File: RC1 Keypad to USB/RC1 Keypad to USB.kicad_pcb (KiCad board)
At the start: 2 copper layers, 72.4 x 45.1 mm, 8 parts, among them J1 RC1 Keypad Port, J2 Anchor, SW1 RESET

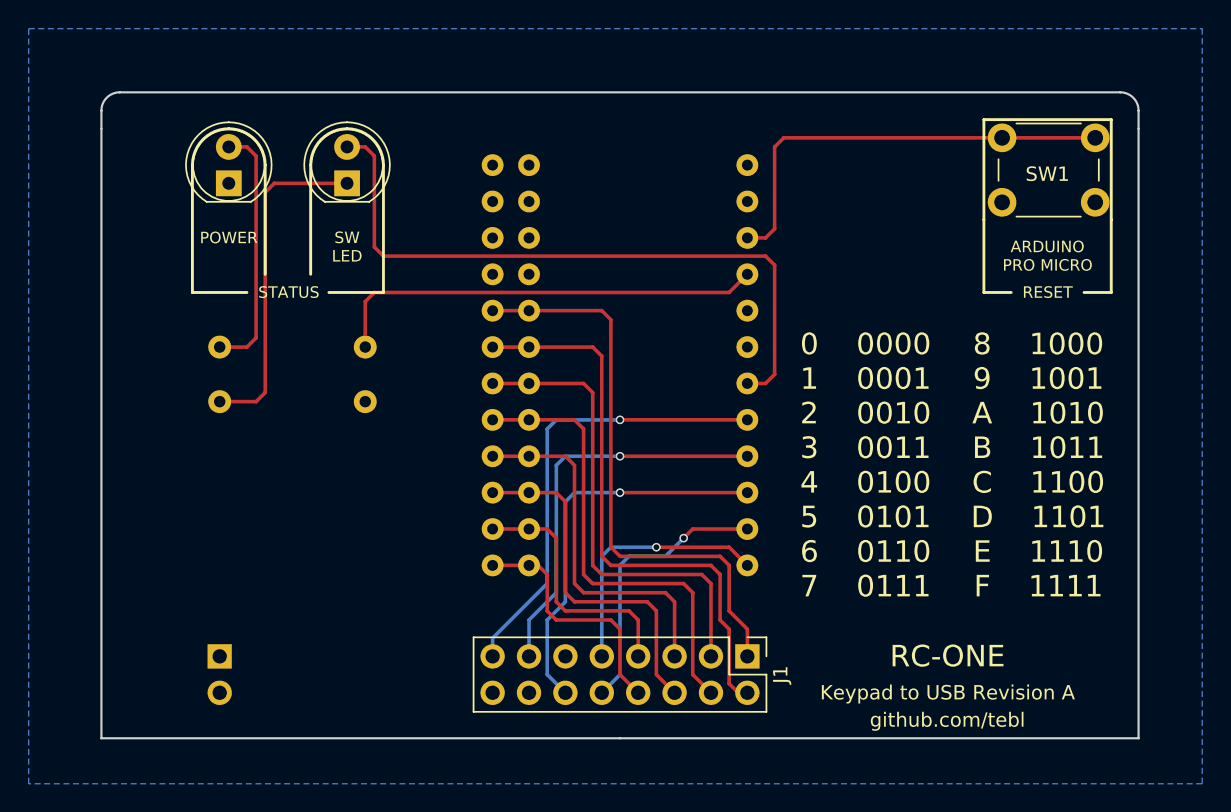
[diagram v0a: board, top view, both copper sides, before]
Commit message: Gerber export keypad to USB module
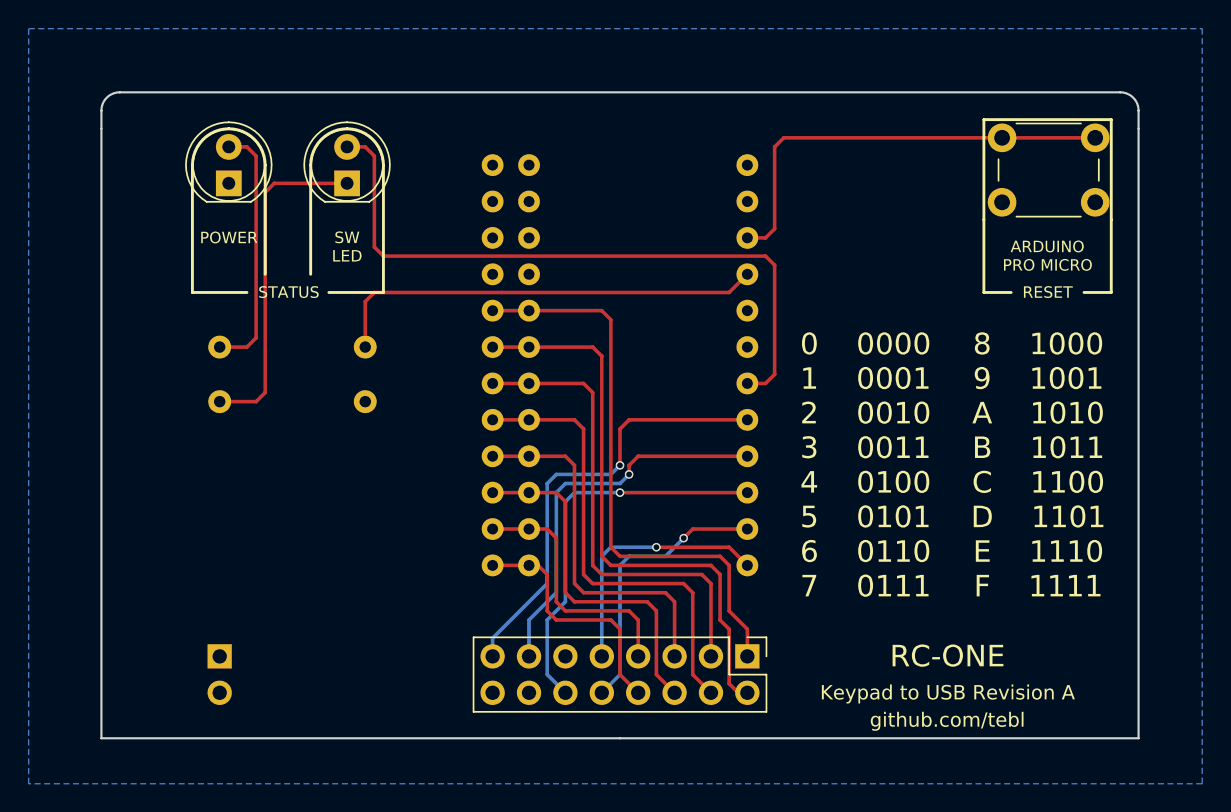
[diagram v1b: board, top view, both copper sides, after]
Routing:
- net /D18: track 31.7 -> 30.9 mm
- net /D15: track 27.7 -> 27.0 mm
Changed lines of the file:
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@@
     (links 37)
     (no_connects 0)
-    (area 112.395 94.615 194.310001 147.320001)
+    (area 117.399999 98.984999 189.940001 144.220001)
     (thickness 1.6)
     (drawings 38)
-    (tracks 145)
+    (tracks 150)
     (zones 0)
     (modules 8)
@@
     (descr "Through hole straight pin header, 2x08, 2.54mm pitch, double rows")
     (tags "Through hole pin header THT 2x08 2.54mm double row")
-    (fp_text reference J1 (at 1.27 -2.33 270) (layer F.SilkS)
+    (fp_text reference J1 (at 1.27 -2.54 270) (layer F.Fab)
       (effects (font (size 1 1) (thickness 0.15)))
     )
@@
     (descr https://www.omron.com/ecb/products/pdf/en-b3f.pdf)
     (tags "tact sw push 6mm")
-    (fp_text reference SW1 (at 3.175 2.54) (layer F.SilkS)
-      (effects (font (size 1 1) (thickness 0.15)))
-    )
-    (fp_text value RESET (at 3.75 6.7) (layer F.Fab)
+    (fp_text reference SW1 (at 3.175 2.54) (layer F.Fab)
+      (effects (font (size 1 1) (thickness 0.15)))
+    )
+    (fp_text value RESET (at 3.175 6.985) (layer F.Fab)
       (effects (font (size 1 1) (thickness 0.15)))
     )
@@
   (segment (start 153.67 139.7) (end 153.67 132.08) (width 0.25) (layer B.Cu) (net 11))
   (via (at 153.67 127) (size 0.6) (drill 0.4) (layers F.Cu B.Cu) (net 12))
-  (segment (start 153.67 127) (end 162.56 127) (width 0.25) (layer F.Cu) (net 12) (status 800000))
+  (segment (start 153.67 127) (end 162.56 127) (width 0.25) (layer F.Cu) (net 12))
   (segment (start 153.67 127) (end 150.495 127) (width 0.25) (layer B.Cu) (net 12))
   (segment (start 148.59 139.7) (end 149.86 140.97) (width 0.25) (layer B.Cu) (net 12))
@@
   (segment (start 149.86 127.635) (end 149.86 134.62) (width 0.25) (layer B.Cu) (net 12))
   (segment (start 150.495 127) (end 149.86 127.635) (width 0.25) (layer B.Cu) (net 12))
-  (via (at 153.67 124.46) (size 0.6) (drill 0.4) (layers F.Cu B.Cu) (net 13))
-  (segment (start 153.67 124.46) (end 162.56 124.46) (width 0.25) (layer F.Cu) (net 13) (status 800000))
+  (segment (start 149.225 127) (end 149.86 126.365) (width 0.25) (layer B.Cu) (net 13))
+  (segment (start 154.305 125.095) (end 154.94 124.46) (width 0.25) (layer F.Cu) (net 13))
+  (segment (start 154.305 125.73) (end 154.305 125.095) (width 0.25) (layer F.Cu) (net 13))
+  (via (at 154.305 125.73) (size 0.6) (drill 0.4) (layers F.Cu B.Cu) (net 13))
+  (segment (start 153.67 126.365) (end 154.305 125.73) (width 0.25) (layer B.Cu) (net 13))
+  (segment (start 149.86 126.365) (end 153.67 126.365) (width 0.25) (layer B.Cu) (net 13))
+  (segment (start 154.94 124.46) (end 162.56 124.46) (width 0.25) (layer F.Cu) (net 13))
   (segment (start 148.59 134.62) (end 147.32 135.89) (width 0.25) (layer B.Cu) (net 13))
   (segment (start 147.32 138.43) (end 147.32 135.89) (width 0.25) (layer B.Cu) (net 13))
-  (segment (start 149.86 124.46) (end 153.67 124.46) (width 0.25) (layer B.Cu) (net 13))
-  (segment (start 149.225 125.095) (end 149.86 124.46) (width 0.25) (layer B.Cu) (net 13))
-  (segment (start 149.225 133.985) (end 149.225 125.095) (width 0.25) (layer B.Cu) (net 13))
+  (segment (start 149.225 133.985) (end 149.225 127) (width 0.25) (layer B.Cu) (net 13))
   (segment (start 148.59 134.62) (end 149.225 133.985) (width 0.25) (layer B.Cu) (net 13))
+  (segment (start 148.59 126.365) (end 149.225 125.73) (width 0.25) (layer B.Cu) (net 14))
+  (segment (start 153.67 122.555) (end 154.305 121.92) (width 0.25) (layer F.Cu) (net 14))
+  (segment (start 153.67 125.095) (end 153.67 122.555) (width 0.25) (layer F.Cu) (net 14))
+  (via (at 153.67 125.095) (size 0.6) (drill 0.4) (layers F.Cu B.Cu) (net 14))
+  (segment (start 153.035 125.73) (end 153.67 125.095) (width 0.25) (layer B.Cu) (net 14))
+  (segment (start 149.225 125.73) (end 153.035 125.73) (width 0.25) (layer B.Cu) (net 14))
   (segment (start 147.955 133.985) (end 144.78 137.16) (width 0.25) (layer B.Cu) (net 14))
-  (segment (start 162.56 121.92) (end 153.67 121.92) (width 0.25) (layer F.Cu) (net 14))
+  (segment (start 162.56 121.92) (end 154.305 121.92) (width 0.25) (layer F.Cu) (net 14))
   (segment (start 144.78 137.16) (end 144.78 138.43) (width 0.25) (layer B.Cu) (net 14))
   (segment (start 148.59 133.35) (end 147.955 133.985) (width 0.25) (layer B.Cu) (net 14))
-  (segment (start 148.59 122.555) (end 148.59 133.35) (width 0.25) (layer B.Cu) (net 14))
-  (segment (start 149.225 121.92) (end 148.59 122.555) (width 0.25) (layer B.Cu) (net 14))
-  (segment (start 149.86 121.92) (end 149.225 121.92) (width 0.25) (layer B.Cu) (net 14))
-  (segment (start 153.67 121.92) (end 149.86 121.92) (width 0.25) (layer B.Cu) (net 14))
-  (via (at 153.67 121.92) (size 0.6) (drill 0.4) (layers F.Cu B.Cu) (net 14))
+  (segment (start 148.59 126.365) (end 148.59 133.35) (width 0.25) (layer B.Cu) (net 14))
   (segment (start 162.56 119.38) (end 163.83 119.38) (width 0.25) (layer F.Cu) (net 15))
   (segment (start 135.89 102.87) (end 134.62 102.87) (width 0.25) (layer F.Cu) (net 15))

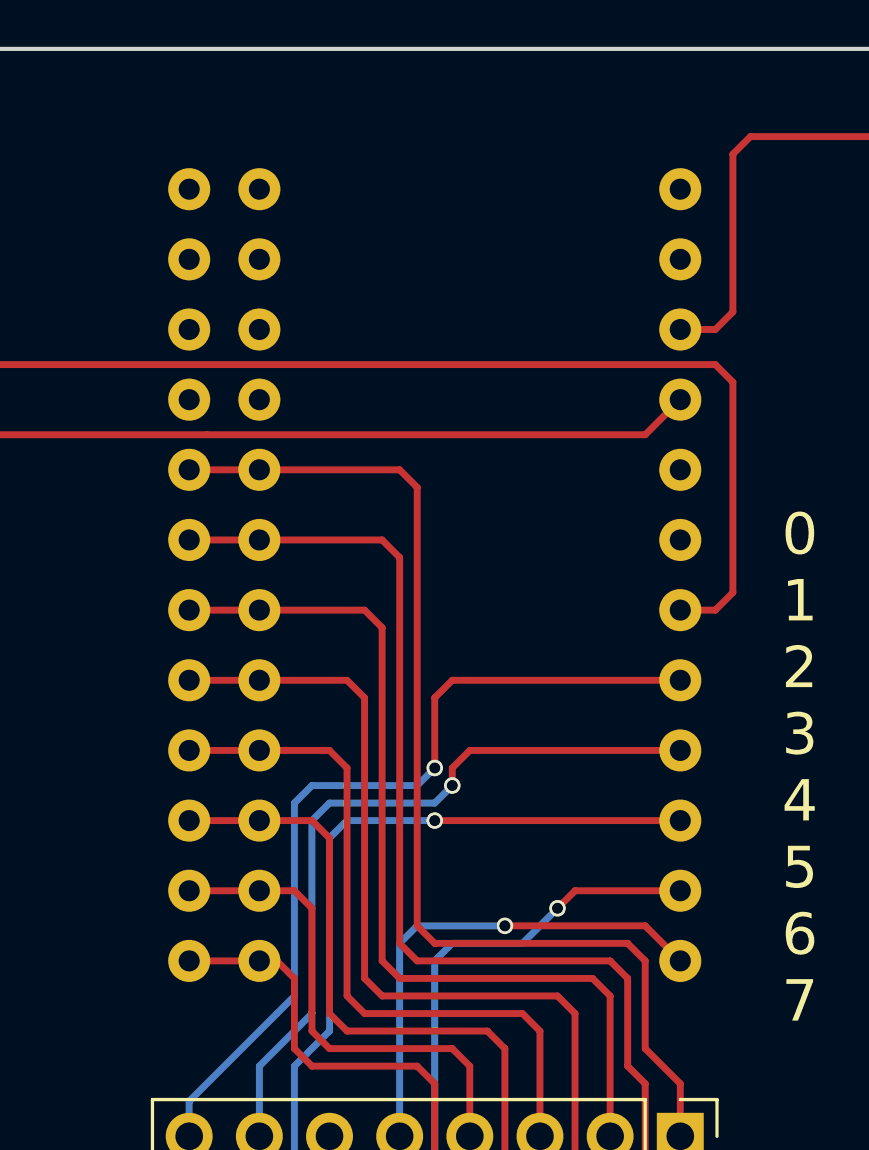
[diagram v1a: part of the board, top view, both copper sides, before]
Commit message: Updated pad dimensions for Arduino Pro Micro
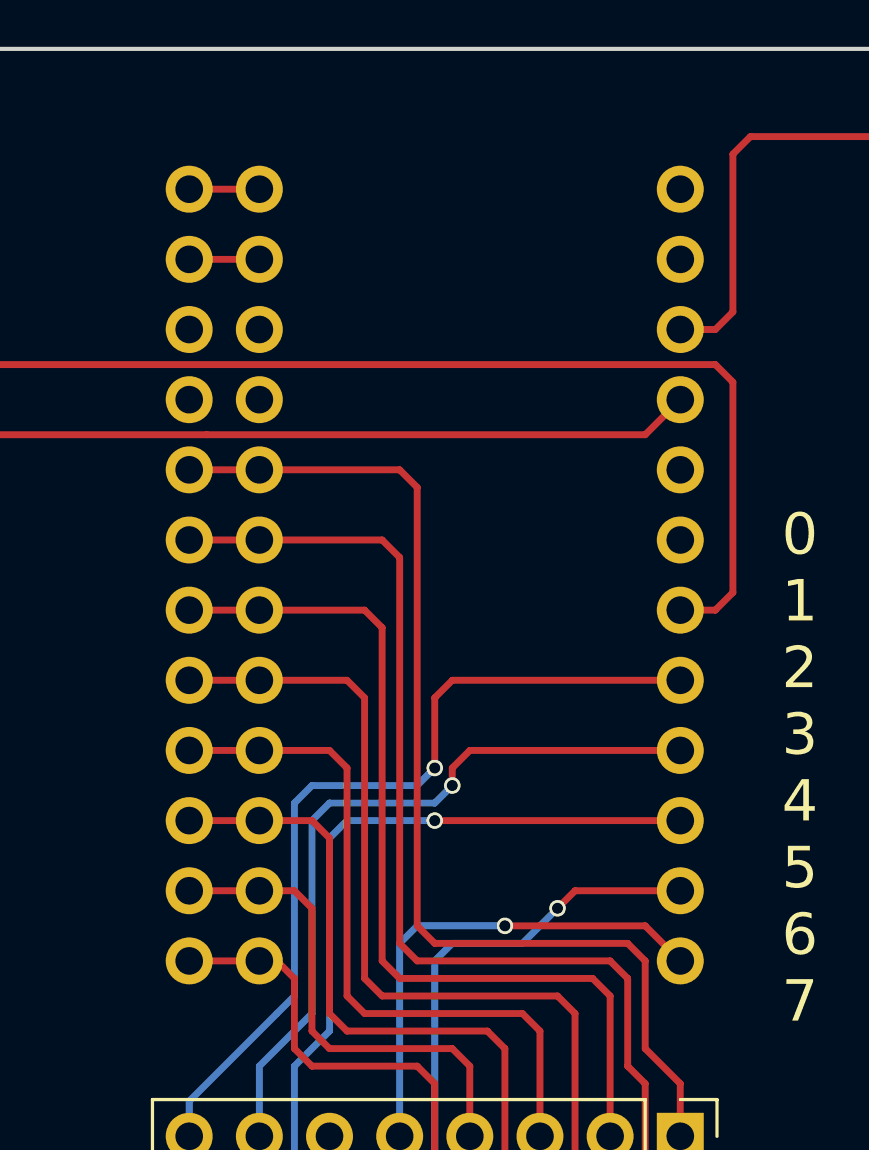
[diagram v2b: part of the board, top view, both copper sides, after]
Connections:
- A1 pad 1: (no net) -> Net-(A1-Pad1)
- A1 pad 2: (no net) -> Net-(A1-Pad2)
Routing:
- net Net-(A1-Pad2): track 0.00 -> 2.54 mm
- net Net-(A1-Pad1): track 0.00 -> 2.54 mm
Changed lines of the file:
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@@
 (kicad_pcb (version 4) (host pcbnew 4.0.7)
   (general
-    (links 37)
+    (links 39)
     (no_connects 0)
     (area 117.399999 98.984999 189.940001 144.220001)
     (thickness 1.6)
     (drawings 38)
-    (tracks 150)
+    (tracks 152)
     (zones 0)
     (modules 8)
-    (nets 20)
+    (nets 22)
   )
   (page A4)
@@
   (net 18 "Net-(D1-Pad2)")
   (net 19 "Net-(D2-Pad1)")
+  (net 20 "Net-(A1-Pad2)")
+  (net 21 "Net-(A1-Pad1)")
   (net_class Default "This is the default net class."
     (clearance 0.2)
@@
     (add_net /D9)
     (add_net GND)
+    (add_net "Net-(A1-Pad1)")
     (add_net "Net-(A1-Pad18)")
+    (add_net "Net-(A1-Pad2)")
     (add_net "Net-(A1-Pad21)")
     (add_net "Net-(A1-Pad22)")
@@
     (fp_line (start -10.16 -17.78) (end -10.16 16.51) (layer B.SilkS) (width 0.15))
     (fp_line (start -10.16 16.51) (end 10.16 16.51) (layer B.SilkS) (width 0.15))
-    (pad 12 thru_hole circle (at -6.35 13.97) (size 1.524 1.524) (drill 0.762) (layers *.Cu *.Mask)
+    (pad 12 thru_hole circle (at -6.35 13.97) (size 1.7 1.7) (drill 1) (layers *.Cu *.Mask)
       (net 9 /D9))
-    (pad 11 thru_hole circle (at -6.35 11.43) (size 1.524 1.524) (drill 0.762) (layers *.Cu *.Mask)
+    (pad 11 thru_hole circle (at -6.35 11.43) (size 1.7 1.7) (drill 1) (layers *.Cu *.Mask)
       (net 8 /D8))
-    (pad 10 thru_hole circle (at -6.35 8.89) (size 1.524 1.524) (drill 0.762) (layers *.Cu *.Mask)
+    (pad 10 thru_hole circle (at -6.35 8.89) (size 1.7 1.7) (drill 1) (layers *.Cu *.Mask)
       (net 7 /D7))
-    (pad 9 thru_hole circle (at -6.35 6.35) (size 1.524 1.524) (drill 0.762) (layers *.Cu *.Mask)
+    (pad 9 thru_hole circle (at -6.35 6.35) (size 1.7 1.7) (drill 1) (layers *.Cu *.Mask)
       (net 6 /D6))
-    (pad 8 thru_hole circle (at -6.35 3.81) (size 1.524 1.524) (drill 0.762) (layers *.Cu *.Mask)
+    (pad 8 thru_hole circle (at -6.35 3.81) (size 1.7 1.7) (drill 1) (layers *.Cu *.Mask)
       (net 5 /D5))
-    (pad 7 thru_hole circle (at -6.35 1.27) (size 1.524 1.524) (drill 0.762) (layers *.Cu *.Mask)
+    (pad 7 thru_hole circle (at -6.35 1.27) (size 1.7 1.7) (drill 1) (layers *.Cu *.Mask)
       (net 4 /D4))
-    (pad 6 thru_hole circle (at -6.35 -1.27) (size 1.524 1.524) (drill 0.762) (layers *.Cu *.Mask)
+    (pad 6 thru_hole circle (at -6.35 -1.27) (size 1.7 1.7) (drill 1) (layers *.Cu *.Mask)
       (net 3 /D3))
-    (pad 5 thru_hole circle (at -6.35 -3.81) (size 1.524 1.524) (drill 0.762) (layers *.Cu *.Mask)
+    (pad 5 thru_hole circle (at -6.35 -3.81) (size 1.7 1.7) (drill 1) (layers *.Cu *.Mask)
       (net 2 /D2))
-    (pad 4 thru_hole circle (at -6.35 -6.35) (size 1.524 1.524) (drill 0.762) (layers *.Cu *.Mask)
-      (net 1 GND))
-    (pad 3 thru_hole circle (at -6.35 -8.89) (size 1.524 1.524) (drill 0.762) (layers *.Cu *.Mask)
-      (net 1 GND))
-    (pad 2 thru_hole circle (at -6.35 -11.43) (size 1.524 1.524) (drill 0.762) (layers *.Cu *.Mask))
-    (pad 1 thru_hole circle (at -6.35 -13.97) (size 1.524 1.524) (drill 0.762) (layers *.Cu *.Mask))
-    (pad 2 thru_hole circle (at -8.89 -11.43) (size 1.524 1.524) (drill 0.762) (layers *.Cu *.Mask))
-    (pad 3 thru_hole circle (at -8.89 -8.89) (size 1.524 1.524) (drill 0.762) (layers *.Cu *.Mask)
-      (net 1 GND))
-    (pad 4 thru_hole circle (at -8.89 -6.35) (size 1.524 1.524) (drill 0.762) (layers *.Cu *.Mask)
-      (net 1 GND))
-    (pad 5 thru_hole circle (at -8.89 -3.81) (size 1.524 1.524) (drill 0.762) (layers *.Cu *.Mask)
+    (pad 4 thru_hole circle (at -6.35 -6.35) (size 1.7 1.7) (drill 1) (layers *.Cu *.Mask)
+      (net 1 GND))
+    (pad 3 thru_hole circle (at -6.35 -8.89) (size 1.7 1.7) (drill 1) (layers *.Cu *.Mask)
+      (net 1 GND))
+    (pad 2 thru_hole circle (at -6.35 -11.43) (size 1.7 1.7) (drill 1) (layers *.Cu *.Mask)
+      (net 20 "Net-(A1-Pad2)"))
+    (pad 1 thru_hole circle (at -6.35 -13.97) (size 1.7 1.7) (drill 1) (layers *.Cu *.Mask)
+      (net 21 "Net-(A1-Pad1)"))
+    (pad 2 thru_hole circle (at -8.89 -11.43) (size 1.7 1.7) (drill 1) (layers *.Cu *.Mask)
+      (net 20 "Net-(A1-Pad2)"))
+    (pad 3 thru_hole circle (at -8.89 -8.89) (size 1.7 1.7) (drill 1) (layers *.Cu *.Mask)
+      (net 1 GND))
+    (pad 4 thru_hole circle (at -8.89 -6.35) (size 1.7 1.7) (drill 1) (layers *.Cu *.Mask)
+      (net 1 GND))
+    (pad 5 thru_hole circle (at -8.89 -3.81) (size 1.7 1.7) (drill 1) (layers *.Cu *.Mask)
       (net 2 /D2))
-    (pad 6 thru_hole circle (at -8.89 -1.27) (size 1.524 1.524) (drill 0.762) (layers *.Cu *.Mask)
+    (pad 6 thru_hole circle (at -8.89 -1.27) (size 1.7 1.7) (drill 1) (layers *.Cu *.Mask)
       (net 3 /D3))
-    (pad 7 thru_hole circle (at -8.89 1.27) (size 1.524 1.524) (drill 0.762) (layers *.Cu *.Mask)
+    (pad 7 thru_hole circle (at -8.89 1.27) (size 1.7 1.7) (drill 1) (layers *.Cu *.Mask)
       (net 4 /D4))
-    (pad 8 thru_hole circle (at -8.89 3.81) (size 1.524 1.524) (drill 0.762) (layers *.Cu *.Mask)
+    (pad 8 thru_hole circle (at -8.89 3.81) (size 1.7 1.7) (drill 1) (layers *.Cu *.Mask)
       (net 5 /D5))
-    (pad 9 thru_hole circle (at -8.89 6.35) (size 1.524 1.524) (drill 0.762) (layers *.Cu *.Mask)
+    (pad 9 thru_hole circle (at -8.89 6.35) (size 1.7 1.7) (drill 1) (layers *.Cu *.Mask)
       (net 6 /D6))
-    (pad 10 thru_hole circle (at -8.89 8.89) (size 1.524 1.524) (drill 0.762) (layers *.Cu *.Mask)
+    (pad 10 thru_hole circle (at -8.89 8.89) (size 1.7 1.7) (drill 1) (layers *.Cu *.Mask)
       (net 7 /D7))
-    (pad 11 thru_hole circle (at -8.89 11.43) (size 1.524 1.524) (drill 0.762) (layers *.Cu *.Mask)
+    (pad 11 thru_hole circle (at -8.89 11.43) (size 1.7 1.7) (drill 1) (layers *.Cu *.Mask)
       (net 8 /D8))
-    (pad 12 thru_hole circle (at -8.89 13.97) (size 1.524 1.524) (drill 0.762) (layers *.Cu *.Mask)
+    (pad 12 thru_hole circle (at -8.89 13.97) (size 1.7 1.7) (drill 1) (layers *.Cu *.Mask)
       (net 9 /D9))
-    (pad 13 thru_hole circle (at 8.89 13.97) (size 1.524 1.524) (drill 0.762) (layers *.Cu *.Mask)
+    (pad 13 thru_hole circle (at 8.89 13.97) (size 1.7 1.7) (drill 1) (layers *.Cu *.Mask)
       (net 10 /D10))
-    (pad 14 thru_hole circle (at 8.89 11.43) (size 1.524 1.524) (drill 0.762) (layers *.Cu *.Mask)
+    (pad 14 thru_hole circle (at 8.89 11.43) (size 1.7 1.7) (drill 1) (layers *.Cu *.Mask)
       (net 11 /D16))
-    (pad 15 thru_hole circle (at 8.89 8.89) (size 1.524 1.524) (drill 0.762) (layers *.Cu *.Mask)
+    (pad 15 thru_hole circle (at 8.89 8.89) (size 1.7 1.7) (drill 1) (layers *.Cu *.Mask)
       (net 12 /D14))
-    (pad 16 thru_hole circle (at 8.89 6.35) (size 1.524 1.524) (drill 0.762) (layers *.Cu *.Mask)
+    (pad 16 thru_hole circle (at 8.89 6.35) (size 1.7 1.7) (drill 1) (layers *.Cu *.Mask)
       (net 13 /D15))
-    (pad 17 thru_hole circle (at 8.89 3.81) (size 1.524 1.524) (drill 0.762) (layers *.Cu *.Mask)
+    (pad 17 thru_hole circle (at 8.89 3.81) (size 1.7 1.7) (drill 1) (layers *.Cu *.Mask)
       (net 14 /D18))
-    (pad 18 thru_hole circle (at 8.89 1.27) (size 1.524 1.524) (drill 0.762) (layers *.Cu *.Mask)
+    (pad 18 thru_hole circle (at 8.89 1.27) (size 1.7 1.7) (drill 1) (layers *.Cu *.Mask)
       (net 15 "Net-(A1-Pad18)"))
-    (pad 19 thru_hole circle (at 8.89 -1.27) (size 1.524 1.524) (drill 0.762) (layers *.Cu *.Mask))
-    (pad 20 thru_hole circle (at 8.89 -3.81) (size 1.524 1.524) (drill 0.762) (layers *.Cu *.Mask))
-    (pad 21 thru_hole circle (at 8.89 -6.35) (size 1.524 1.524) (drill 0.762) (layers *.Cu *.Mask)
+    (pad 19 thru_hole circle (at 8.89 -1.27) (size 1.7 1.7) (drill 1) (layers *.Cu *.Mask))
+    (pad 20 thru_hole circle (at 8.89 -3.81) (size 1.7 1.7) (drill 1) (layers *.Cu *.Mask))
+    (pad 21 thru_hole circle (at 8.89 -6.35) (size 1.7 1.7) (drill 1) (layers *.Cu *.Mask)
       (net 16 "Net-(A1-Pad21)"))
-    (pad 22 thru_hole circle (at 8.89 -8.89) (size 1.524 1.524) (drill 0.762) (layers *.Cu *.Mask)
+    (pad 22 thru_hole circle (at 8.89 -8.89) (size 1.7 1.7) (drill 1) (layers *.Cu *.Mask)
       (net 17 "Net-(A1-Pad22)"))
-    (pad 23 thru_hole circle (at 8.89 -11.43) (size 1.524 1.524) (drill 0.762) (layers *.Cu *.Mask)
-      (net 1 GND))
-    (pad 24 thru_hole circle (at 8.89 -13.97) (size 1.524 1.524) (drill 0.762) (layers *.Cu *.Mask))
-    (pad 1 thru_hole circle (at -8.89 -13.97) (size 1.524 1.524) (drill 0.762) (layers *.Cu *.Mask))
+    (pad 23 thru_hole circle (at 8.89 -11.43) (size 1.7 1.7) (drill 1) (layers *.Cu *.Mask)
+      (net 1 GND))
+    (pad 24 thru_hole circle (at 8.89 -13.97) (size 1.7 1.7) (drill 1) (layers *.Cu *.Mask))
+    (pad 1 thru_hole circle (at -8.89 -13.97) (size 1.7 1.7) (drill 1) (layers *.Cu *.Mask)
+      (net 21 "Net-(A1-Pad1)"))
   )
   (gr_text github.com/tebl (at 176.53 142.875) (layer F.SilkS)
@@
   (segment (start 128.905 120.015) (end 128.905 106.045) (width 0.25) (layer F.Cu) (net 19))
   (segment (start 128.27 120.65) (end 128.905 120.015) (width 0.25) (layer F.Cu) (net 19))
+  (segment (start 147.32 106.68) (end 144.78 106.68) (width 0.25) (layer F.Cu) (net 20))
+  (segment (start 144.78 104.14) (end 147.32 104.14) (width 0.25) (layer F.Cu) (net 21))
   (zone (net 1) (net_name GND) (layer B.Cu) (hatch edge 0.508)
     (connect_pads (clearance 0.508))
